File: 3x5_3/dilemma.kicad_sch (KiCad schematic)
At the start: 173 parts, among them J5001 USB_C_Receptacle_USB2.0, J5002 NA_Conn_01x02, J5003 NA_serial, J5004 NA_GC9A01, J5005 NA_Conn_01x04_Female, J5007 Cirque, J5008 Conn_01x05, J5009 Conn_01x05, J5011 BATTERY_CONN_DEANS, SW101 NA_SW_Push, SW102 NA_SW_Push, SW103 NA_SW_Push, SW104 NA_SW_Push, SW105 NA_SW_Push, SW106 NA_SW_Push, SW107 NA_SW_Push, SW108 NA_SW_Push, SW109 NA_SW_Push, SW112 NA_SW_Push, SW113 NA_SW_Push, SW114 NA_SW_Push, SW115 NA_SW_Push, SW116 NA_SW_Push, SW117 NA_SW_Push, SW118 NA_SW_Push, SW119 NA_SW_Push, SW3001 NA_SW_Push, SW5001 SW_Push, SW5002 NA_SW_Push, SW5003 NA_SW_Push, SW5004 NA_SW_Push, SW5005 NA_SW_Push, SW5006 NA_SW_Push, SW5007 NA_SW_Push, SW5008 NA_SW_Push, SW5009 NA_SW_Push, SW5010 NA_SW_Push, SW5011 NA_SW_Push, SW5012 NA_SW_Push, SW5013 NA_SW_Push, SW5014 NA_SW_Push, SW5015 NA_SW_Push, SW5016 NA_SW_Push, SW5017 NA_SW_Push, SW5018 NA_SW_Push, SW5019 NA_SW_Push, SW5020 NA_RotaryEncoder_Switch, SW5021 SW_SPST, SW5022 SW_SPST, U5001 XC6210B332MR-G, U5002 RP2040, U5003 USBLC6-2P6, U5004 W25Q128JVS, U5006 USBLC6-2P6, U5007 eliteC, Y5001 Crystal_GND24

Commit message: left side schematic
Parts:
- removed C5001, C5002: 1µ, Capacitor_SMD:C_0603_1608Metric, symbol Device:C
- removed C5003, C5004, C5016, C5018: 1µ, Capacitor_SMD:C_0402_1005Metric, symbol Device:C
- removed C5005, C5008: 15p, Capacitor_SMD:C_0402_1005Metric, symbol Device:C
- removed C5006, C5007, C5009, C5010, C5011, C5012, C5013, C5014: 100n, Capacitor_SMD:C_0402_1005Metric, symbol Device:C
- removed D5001: LED, LED_SMD:LED_0402_1005Metric, symbol Device:LED
- removed D5002, D5003, D5005, D5006, D5007, D5008, D5010, D5012: D_CC, local-libraries:SOT-323_SC-70, symbol Device:D_Dual_CommonCathode_AAK
- removed D5004: B5817, Diode_SMD:D_SOD-323, symbol Device:D_Schottky
- removed D5013, D5014, D5015, D5016, D5017, D5018, D5019, D5020, D5021, D5022, D5023, D5024, D5025, D5026, D5027, D5028, D5029, D5030: SK6805-EC15, 0xB2_drawings:LED_SK6805-EC15_1.5x1.5mm_P0.6mm_handsolder(1), symbol sk6805-ec15:SK6805-EC15
- removed D5049, D5050, D5051, D5052, D5053, D5054, D5055, D5056, D5057, D5058, D5059, D5060, D5061, D5062, D5063, D5064, D5065, D5066: SK6812MINI, local-libraries:SK6812_mini_e_corners, symbol LED:SK6812MINI
- removed F5001: Polyfuse, Fuse:Fuse_0603_1608Metric, symbol Device:Polyfuse
- removed FB5001: FerriteBead_Small, Inductor_SMD:L_0603_1608Metric, symbol Device:FerriteBead_Small
- removed J5001: USB_C_Receptacle_USB2.0, 0xLib_USB_Type-C:USB_C_Receptacle_HRO_TYPE-C-31-M-13B, symbol Connector:USB_C_Receptacle_USB2.0
- removed J5002: NA_Conn_01x02, Connector_PinHeader_1.27mm:PinHeader_1x02_P1.27mm_Vertical, symbol Connector_Generic:Conn_01x02
- removed J5003: NA_serial, local-libraries:Jack_3.5mm_PJ320E_Horizontal, symbol Connector:AudioJack4
- removed J5004: NA_GC9A01, local-libraries:PinHeader_1x07_P2.54mm_Vertical, symbol kbd:IPS_LCD__gc9a01_240X240
- removed J5005: NA_Conn_01x04_Female, local-libraries:PinHeader_1x04_P2.54mm_Vertical_debug, symbol Connector:Conn_01x04_Female
- removed J5007: Cirque, local-libraries:FPC-SMD_FPC05012-09200-.5mm, symbol Connector:Conn_01x14_Female
- removed J5008, J5009: Conn_01x05, local-libraries:PinHeader_1x05_P1.27mm_Vertical_SMD, symbol Connector_Generic:Conn_01x05
- removed O5001: NA_OLED, local-libraries:PinHeader_1x04_P2.54mm_Vertical, symbol Connector_Generic:Conn_01x04
- removed R5001, R5003, R5008: 1k, Resistor_SMD:R_0402_1005Metric, symbol Device:R
- removed R5002, R5010, R5011: 10k, Resistor_SMD:R_0402_1005Metric, symbol Device:R
- removed R5004, R5005, R5009: 5.1k, Resistor_SMD:R_0402_1005Metric, symbol Device:R
- removed R5006, R5007: 27, Resistor_SMD:R_0402_1005Metric, symbol Device:R
- removed R5012: 5.1k, local-libraries:R_0402_1005Metric_nolabel, symbol Device:R
- removed R5013, R5014: 4.7k, local-libraries:R_0402_1005Metric_nolabel, symbol Device:R
- removed R5015: 330, Resistor_SMD:R_0402_1005Metric, symbol Device:R
- removed SW5001: SW_Push, Button_Switch_SMD:SW_SPST_CK_KXT3, symbol Switch:SW_Push
- removed SW5020: NA_RotaryEncoder_Switch, local-libraries:RotaryEncoder_Alps_EC11E-Switch_Vertical_H20mm_roundholes, symbol Device:RotaryEncoder_Switch
- removed U5001: XC6210B332MR-G, Package_TO_SOT_SMD:SOT-23-5, symbol Regulator_Linear:AP2127K-3.3
- removed U5002: RP2040, 0xLib_Package_DFN_QFN:QFN-56-1EP_7x7mm_P0.4mm_EP3.2x3.2mm, symbol MCU_RaspberryPi_RP2040:RP2040
- removed U5003, U5006: USBLC6-2P6, Package_TO_SOT_SMD:SOT-666, symbol Power_Protection:USBLC6-2P6
- removed U5004: W25Q128JVS, drawings:W25Q128JVPIQ, symbol Memory_Flash:W25Q128JVS
- removed Y5001: Crystal_GND24, Crystal:Crystal_SMD_2520-4Pin_2.5x2.0mm, symbol Device:Crystal_GND24
- added D5001, D5002, D5003, D5004, D5005, D5006, D5007, D5008, D5010, D5012, D5013, D5014, D5015, D5016, D5017, D5018: D, local-libraries:D_SOD-323, symbol Device:D
- added J5001: BATTERY_CONN_DEANS, local-libraries:battery_connector_THT, symbol SparkFun-Connectors:BATTERY_CONN_DEANS
- added PSW5002: SW_DPDT_x2, local-libraries:Switch_MSK-12C01-07, symbol jiran-ble:SW_DPDT
- added U5001: eliteC, local-libraries:Sparkfun_Pro_Micro, symbol elite-C:eliteC
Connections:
- net GND_L is gone; now on net GND: H5001.1, H5002.1, H5003.1, H5004.1, H5005.1, H5006.1, H5007.1, H5008.1, SW5021.2 (B)
- net +5VL: now also U5001.21 (VCC)
- net GND: now also J5001.-, U5001.23 (GND), U5001.3 (GND), U5001.4 (GND)
- net M_COL1_L: now also D5001.1 (K), D5002.1 (K), D5003.1 (K), D5004.1 (K), U5001.11 (B4)
- net M_COL2_L: now also D5005.1 (K), D5006.1 (K), D5007.1 (K), D5008.1 (K), U5001.12 (B5)
- net M_COL3_L: now also D5010.1 (K), D5012.1 (K), D5013.1 (K), D5014.1 (K), U5001.10 (E6)
- net M_COL4_L: now also D5015.1 (K), D5016.1 (K), U5001.9 (D7)
- net M_COL5_L: now also D5017.1 (K), D5018.1 (K), U5001.18 (F6)
- net M_ROW1_L: now also U5001.17 (F7)
- net M_ROW2_L: now also U5001.7 (D4)
- net M_ROW3_L: now also U5001.8 (C6)
- net M_ROW4_L: now also U5001.19 (F5)
- net at SW5003.2: now also D5002.2 (A)
- net at SW5011.2: now also D5012.2 (A)
- net at SW5010.2: now also D5010.2 (A)
- net at SW5012.2: now also D5013.2 (A)
- net at SW5005.2: now also D5004.2 (A)
- net at SW5004.2: now also D5003.2 (A)
- net at SW5009.2: now also D5008.2 (A)
- net at SW5018.2: now also D5018.2 (A)
- net at SW5017.2: now also D5017.2 (A)
- net at SW5002.2: now also D5001.2 (A)
- net at SW5014.2: now also D5015.2 (A)
- net at SW5007.2: now also D5006.2 (A)
- net at SW5006.2: now also D5005.2 (A)
- net at SW5015.2: now also D5016.2 (A)
- net at SW5008.2: now also D5007.2 (A)
- net encoder_diode_L: no longer names the net of SW5013.2
- net encoder_diode_L: now also D5014.2 (A)
- net ~{RESET_L} renamed RESET_L
- net RESET_L: now also U5001.22 (RST)
- new net BAT_L: PSW5002.1 (A), U5001.24 (RAW)
- new net BAT_SW_L: J5001.+, PSW5002.2 (B)
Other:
- note added: "Left"
- note added: "Right"
- note removed: "Breakout"
- note removed: "Cirque FPC connector"
- note removed: "Debug breakout"
- note removed: "Decoupling"
- note removed: "ESD protection"
- note removed: "Flash memory"
- note removed: "Handedness"
- note removed: "Indicator & buttons"
- note removed: "LCD"
- note removed: "OLED connector"
- note removed: "Per key RGB"
- note removed: "Rotary encoders"
- note removed: "Serial"
- note removed: "USB-C connector"
- note removed: "Underglow RGB"
- note removed: "Voltage regulation"
- note removed: "switch to gnd for left half"
- moved on the sheet: D112, D115, D5009, D5011, D5031, D5032, D5033, D5034, D5035, D5036, D5037, D5038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

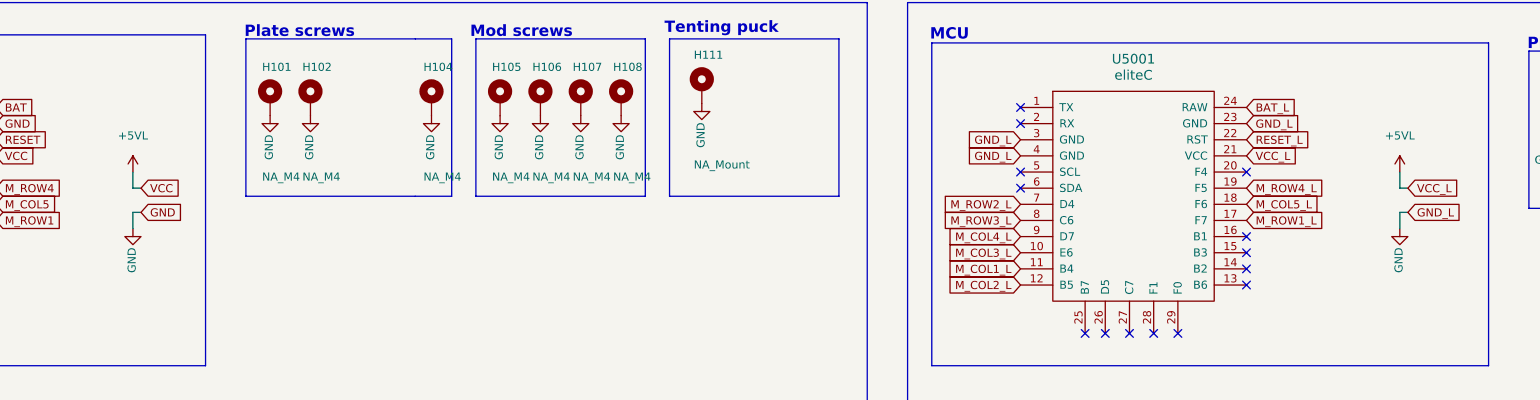
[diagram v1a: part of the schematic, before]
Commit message: right side component placement
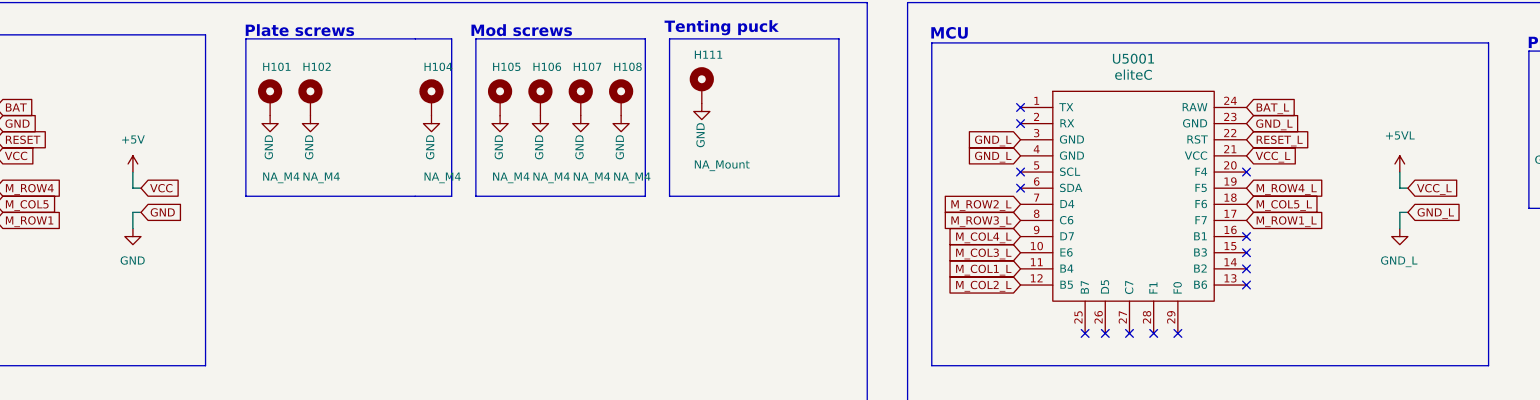
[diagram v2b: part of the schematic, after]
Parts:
- D5001, D5002, D5003, D5004, D5005, D5006, D5007, D5008, D5009, D5010, D5011, D5012, D5013, D5014, D5015, D5016, D5017, D5018: footprint local-libraries:D_SOD-323 -> Diode_SMD:D_SOD-123
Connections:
- net +5VL: no longer U5007.21 (VCC)
- net GND: no longer H5001.1, H5002.1, H5003.1, H5004.1, H5005.1, H5006.1, H5007.1, H5008.1, J5001.-, SW5021.2 (B), U5001.23 (GND), U5001.3 (GND), U5001.4 (GND)
- new net +5V: U5007.21 (VCC)
- new net GND_L: H5001.1, H5002.1, H5003.1, H5004.1, H5005.1, H5006.1, H5007.1, H5008.1, J5001.-, SW5021.2 (B), U5001.23 (GND), U5001.3 (GND), U5001.4 (GND)
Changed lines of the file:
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@@
 			)
 		)
-		(property "Footprint" "local-libraries:D_SOD-323"
+		(property "Footprint" "Diode_SMD:D_SOD-123"
 			(at 312.42 154.94 0)
 			(effects
@@
 			)
 		)
-		(property "Footprint" "local-libraries:D_SOD-323"
+		(property "Footprint" "Diode_SMD:D_SOD-123"
 			(at 339.09 175.26 0)
 			(effects
@@
 			)
 		)
-		(property "Footprint" "local-libraries:D_SOD-323"
+		(property "Footprint" "Diode_SMD:D_SOD-123"
 			(at 259.08 165.1 0)
 			(effects
@@
 			)
 		)
-		(property "Footprint" "local-libraries:D_SOD-323"
+		(property "Footprint" "Diode_SMD:D_SOD-123"
 			(at 312.42 165.1 0)
 			(effects
@@
 			)
 		)
-		(property "Footprint" "local-libraries:D_SOD-323"
+		(property "Footprint" "Diode_SMD:D_SOD-123"
 			(at 339.09 154.94 0)
 			(effects
@@
 			)
 		)
-		(property "Footprint" "local-libraries:D_SOD-323"
+		(property "Footprint" "Diode_SMD:D_SOD-123"
 			(at 285.75 185.42 0)
 			(effects
@@
 		)
 		(property "Value" "GND"
-			(at 90.014 85.7249 90)
+			(at 88.138 83.82 0)
 			(effects
 				(font
@@
 			)
 		)
-		(property "Value" "GND"
-			(at 289.404 85.7249 90)
+		(property "Value" "GND_L"
+			(at 286.512 83.82 0)
 			(effects
 				(font
@@
 			)
 		)
-		(property "Footprint" "local-libraries:D_SOD-323"
+		(property "Footprint" "Diode_SMD:D_SOD-123"
 			(at 365.76 175.26 0)
 			(effects
@@
 			)
 		)
-		(property "Footprint" "local-libraries:D_SOD-323"
+		(property "Footprint" "Diode_SMD:D_SOD-123"
 			(at 259.08 175.26 0)
 			(effects
@@
 			)
 		)
-		(property "Footprint" "local-libraries:D_SOD-323"
+		(property "Footprint" "Diode_SMD:D_SOD-123"
 			(at 312.42 175.26 0)
 			(effects
@@
 			)
 		)
-		(property "Footprint" "local-libraries:D_SOD-323"
+		(property "Footprint" "Diode_SMD:D_SOD-123"
 			(at 312.42 185.42 0)
 			(effects
@@
 			)
 		)
-		(property "Footprint" "local-libraries:D_SOD-323"
+		(property "Footprint" "Diode_SMD:D_SOD-123"
 			(at 285.75 165.1 0)
 			(effects
@@
 			)
 		)
-		(property "Value" "+5VL"
-			(at 90.17 64.135 0)
+		(property "Value" "+5V"
+			(at 90.17 64.77 0)
 			(effects
 				(font
@@
 			)
 		)
-		(property "Footprint" "local-libraries:D_SOD-323"
+		(property "Footprint" "Diode_SMD:D_SOD-123"
 			(at 339.09 165.1 0)
 			(effects
@@
 			)
 		)
-		(property "Footprint" "local-libraries:D_SOD-323"
+		(property "Footprint" "Diode_SMD:D_SOD-123"
 			(at 285.75 175.26 0)
 			(effects
@@
 			)
 		)
-		(property "Footprint" "local-libraries:D_SOD-323"
+		(property "Footprint" "Diode_SMD:D_SOD-123"
 			(at 259.08 154.94 0)
 			(effects
@@
 			)
 		)
-		(property "Footprint" "local-libraries:D_SOD-323"
+		(property "Footprint" "Diode_SMD:D_SOD-123"
 			(at 285.75 154.94 0)
 			(effects
@@
 			)
 		)
-		(property "Footprint" "local-libraries:D_SOD-323"
+		(property "Footprint" "Diode_SMD:D_SOD-123"
 			(at 365.76 165.1 0)
 			(effects
@@
 			)
 		)
-		(property "Footprint" "local-libraries:D_SOD-323"
+		(property "Footprint" "Diode_SMD:D_SOD-123"
 			(at 259.08 185.42 0)
 			(effects
@@
 			)
 		)
-		(property "Footprint" "local-libraries:D_SOD-323"
+		(property "Footprint" "Diode_SMD:D_SOD-123"
 			(at 365.76 154.94 0)
 			(effects

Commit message: right side layout
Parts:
- added BT5001: Battery, 0xB2_drawings:LP602945-PCM-LD-A14348, symbol Device:Battery
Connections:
- net GND_L is gone; now on net GND: H5001.1, H5002.1, H5003.1, H5004.1, H5005.1, H5006.1, H5007.1, H5008.1, J5001.-, SW5021.2 (B), U5001.23 (GND), U5001.3 (GND), U5001.4 (GND)
- net M_COL1_L: now also U5001.14 (B2); no longer U5001.11 (B4)
- net M_COL2_L: now also U5001.13 (B6); no longer U5001.12 (B5)
- net M_COL3_L: now also U5001.15 (B3); no longer U5001.10 (E6)
- net M_COL4_L: now also U5001.16 (B1); no longer U5001.9 (D7)
- net M_COL5_L: now also U5001.8 (C6); no longer U5001.18 (F6)
- net M_ROW1_L: now also U5001.9 (D7); no longer U5001.17 (F7)
- net M_ROW2_L: now also U5001.18 (F6); no longer U5001.7 (D4)
- net M_ROW3_L: now also U5001.17 (F7); no longer U5001.8 (C6)
- net M_ROW4_L: now also U5001.7 (D4); no longer U5001.19 (F5)
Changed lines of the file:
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@@
 	)
 	(no_connect
-		(at 265.43 87.63)
+		(at 229.87 82.55)
 	)
 	(no_connect
@@
 	)
 	(no_connect
+		(at 229.87 87.63)
+	)
+	(no_connect
 		(at 68.58 69.85)
 	)
@@
 	)
 	(no_connect
-		(at 46.355 95.25)
+		(at 265.43 72.39)
 	)
 	(no_connect
-		(at 53.975 95.25)
+		(at 46.355 95.25)
 	)
 	(no_connect
-		(at 265.43 82.55)
+		(at 53.975 95.25)
 	)
 	(no_connect
@@
 	)
 	(no_connect
-		(at 265.43 85.09)
-	)
-	(no_connect
 		(at 43.18 95.25)
 	)
@@
 	)
 	(no_connect
-		(at 265.43 80.01)
+		(at 229.87 72.39)
 	)
 	(no_connect
-		(at 229.87 72.39)
+		(at 229.87 85.09)
 	)
 	(no_connect
@@
 	(global_label "M_ROW2_L"
 		(shape input)
-		(at 229.87 74.93 180)
+		(at 265.43 74.93 0)
 		(effects
 			(font
 				(size 1.27 1.27)
 			)
-			(justify right)
+			(justify left)
 		)
 		(property "Intersheetrefs" "${INTERSHEET_REFS}"
-			(at 158.115 28.575 0)
+			(at 337.185 121.285 0)
 			(effects
 				(font
@@
 	(global_label "M_ROW4_L"
 		(shape input)
-		(at 265.43 72.39 0)
+		(at 229.87 74.93 180)
 		(effects
 			(font
 				(size 1.27 1.27)
 			)
-			(justify left)
+			(justify right)
 		)
 		(property "Intersheetrefs" "${INTERSHEET_REFS}"
-			(at 337.185 155.575 0)
+			(at 158.115 -8.255 0)
 			(effects
 				(font
@@
 	(global_label "M_COL2_L"
 		(shape input)
-		(at 229.87 87.63 180)
+		(at 265.43 87.63 0)
 		(effects
 			(font
 				(size 1.27 1.27)
 			)
-			(justify right)
+			(justify left)
 		)
 		(property "Intersheetrefs" "${INTERSHEET_REFS}"
-			(at 204.47 364.49 0)
+			(at 290.83 -189.23 0)
 			(effects
 				(font
@@
 	(global_label "M_COL3_L"
 		(shape input)
-		(at 229.87 82.55 180)
+		(at 265.43 82.55 0)
 		(effects
 			(font
 				(size 1.27 1.27)
 			)
-			(justify right)
+			(justify left)
 		)
 		(property "Intersheetrefs" "${INTERSHEET_REFS}"
-			(at 204.47 359.41 0)
+			(at 290.83 -194.31 0)
 			(effects
 				(font
@@
 	(global_label "M_ROW3_L"
 		(shape input)
-		(at 229.87 77.47 180)
+		(at 265.43 77.47 0)
 		(effects
 			(font
 				(size 1.27 1.27)
 			)
-			(justify right)
+			(justify left)
 		)
 		(property "Intersheetrefs" "${INTERSHEET_REFS}"
-			(at 158.115 8.89 0)
+			(at 337.185 146.05 0)
 			(effects
 				(font
@@
 	(global_label "M_COL5_L"
 		(shape input)
-		(at 265.43 74.93 0)
+		(at 229.87 77.47 180)
 		(effects
 			(font
 				(size 1.27 1.27)
 			)
-			(justify left)
+			(justify right)
 		)
 		(property "Intersheetrefs" "${INTERSHEET_REFS}"
-			(at 290.83 -201.93 0)
+			(at 204.47 354.33 0)
 			(effects
 				(font
@@
 	(global_label "M_COL4_L"
 		(shape input)
-		(at 229.87 80.01 180)
+		(at 265.43 80.01 0)
 		(effects
 			(font
 				(size 1.27 1.27)
 			)
-			(justify right)
+			(justify left)
 		)
 		(property "Intersheetrefs" "${INTERSHEET_REFS}"
-			(at 204.47 356.87 0)
+			(at 290.83 -196.85 0)
 			(effects
 				(font
@@
 	(global_label "M_ROW1_L"
 		(shape input)
-		(at 265.43 77.47 0)
+		(at 229.87 80.01 180)
 		(effects
 			(font
 				(size 1.27 1.27)
 			)
-			(justify left)
+			(justify right)
 		)
 		(property "Intersheetrefs" "${INTERSHEET_REFS}"
-			(at 342.9 114.3 0)
+			(at 152.4 43.18 0)
 			(effects
 				(font
@@
 	(global_label "M_COL1_L"
 		(shape input)
-		(at 229.87 85.09 180)
+		(at 265.43 85.09 0)
 		(effects
 			(font
 				(size 1.27 1.27)
 			)
-			(justify right)
+			(justify left)
 		)
 		(property "Intersheetrefs" "${INTERSHEET_REFS}"
-			(at 204.47 361.95 0)
+			(at 290.83 -191.77 0)
 			(effects
 				(font
@@
 			)
 		)
-		(property "Value" "GND_L"
-			(at 286.512 83.82 0)
+		(property "Value" "GND"
+			(at 287.528 83.566 0)
 			(effects
 				(font
@@
 					(unit 1)
 				)
+			)
+		)
+	)
+	(symbol
+		(lib_id "Device:Battery")
+		(at 317.5 92.71 0)
+		(unit 1)
+		(exclude_from_sim no)
+		(in_bom yes)
+		(on_board yes)
+		(dnp no)
+		(fields_autoplaced yes)
+		(property "Reference" "BT5001"
+			(at 321.31 90.8684 0)
+			(effects
+				(font
+					(size 1.27 1.27)
+				)
+				(justify left)
+			)
+		)
+		(property "Value" "Battery"
+			(at 321.31 93.4084 0)
+			(effects
+				(font
+					(size 1.27 1.27)
+				)
+				(justify left)
+			)
+		)
+		(property "Footprint" "0xB2_drawings:LP602945-PCM-LD-A14348"
+			(at 317.5 91.186 90)
+			(effects
+				(font
+					(size 1.27 1.27)
+				)
+				(hide yes)
+			)
+		)
+		(property "Datasheet" "~"
+			(at 317.5 91.186 90)
+			(effects
+				(font
+					(size 1.27 1.27)
+				)
+				(hide yes)
+			)
+		)
+		(property "Description" "Multiple-cell battery"
+			(at 317.5 92.71 0)
+			(effects
+				(font
+					(size 1.27 1.27)
+				)
+				(hide yes)
+			)
+		)
+		(pin "1"
+		)
+		(pin "2"
+		)
+		(instances
+			(project "dilemma"
+				(path "/7353e96a-343a-4876-b497-b1d205a14d97"
+					(reference "BT5001")
+					(unit 1)
+				)

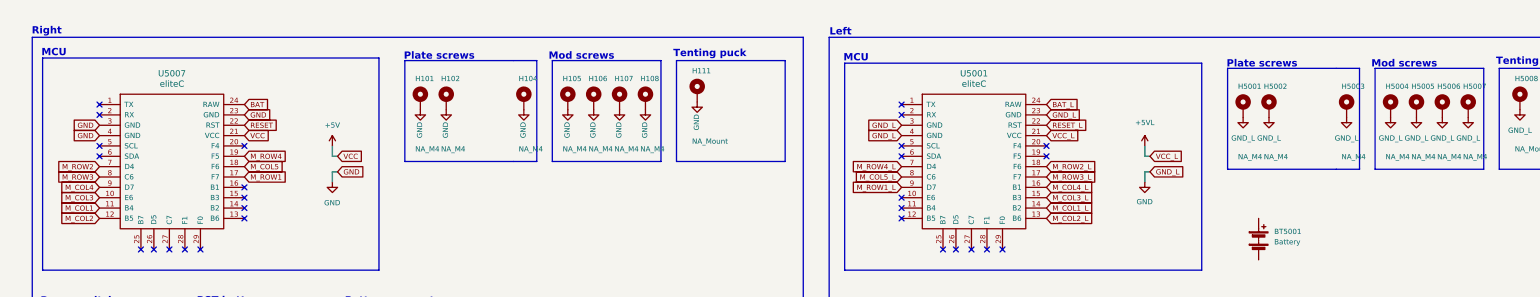
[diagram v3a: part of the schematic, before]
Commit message: adjusted layout for case clearance
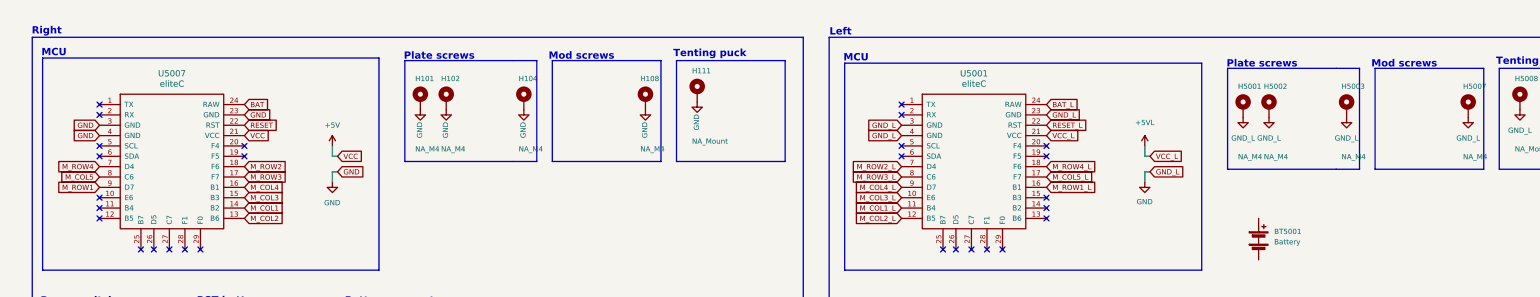
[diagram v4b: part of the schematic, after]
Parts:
- removed H105, H106, H107, H5004, H5005, H5006: NA_M4, local-libraries:MountingHole_3mm_Pad_Via, symbol Mechanical:MountingHole_Pad
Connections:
- net M_COL1: now also U5007.14 (B2); no longer U5007.11 (B4)
- net M_COL1_L: now also U5001.11 (B4); no longer U5001.14 (B2)
- net M_COL2: now also U5007.13 (B6); no longer U5007.12 (B5)
- net M_COL2_L: now also U5001.12 (B5); no longer U5001.13 (B6)
- net M_COL3: now also U5007.15 (B3); no longer U5007.10 (E6)
- net M_COL3_L: now also U5001.10 (E6); no longer U5001.15 (B3)
- net M_COL4: now also U5007.16 (B1); no longer U5007.9 (D7)
- net M_COL4_L: now also U5001.9 (D7); no longer U5001.16 (B1)
- net M_COL5: now also U5007.8 (C6); no longer U5007.18 (F6)
- net M_COL5_L: now also U5001.17 (F7); no longer U5001.8 (C6)
- net M_ROW1: now also U5007.9 (D7); no longer U5007.17 (F7)
- net M_ROW1_L: now also U5001.16 (B1); no longer U5001.9 (D7)
- net M_ROW2: now also U5007.18 (F6); no longer U5007.7 (D4)
- net M_ROW2_L: now also U5001.7 (D4); no longer U5001.18 (F6)
- net M_ROW3: now also U5007.17 (F7); no longer U5007.8 (C6)
- net M_ROW3_L: now also U5001.8 (C6); no longer U5001.17 (F7)
- net M_ROW4: now also U5007.7 (D4); no longer U5007.19 (F5)
- net M_ROW4_L: now also U5001.18 (F6); no longer U5001.7 (D4)
